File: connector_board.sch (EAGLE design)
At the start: 4 parts, among them X1 0446200002

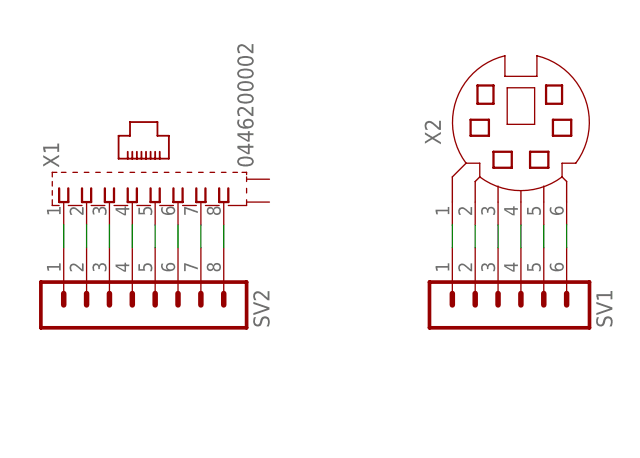
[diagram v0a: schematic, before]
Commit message: added PCBs for extern IO-connections
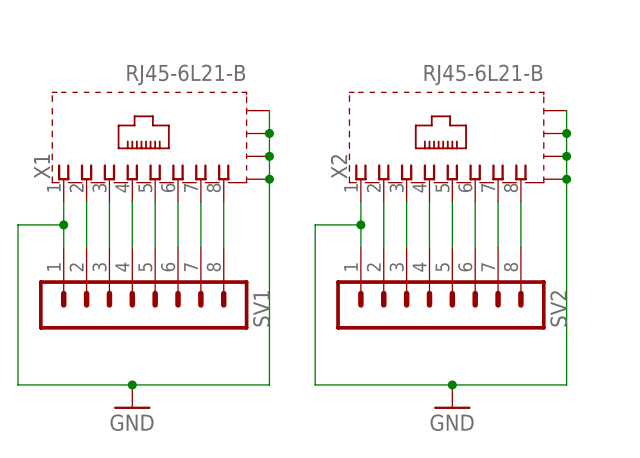
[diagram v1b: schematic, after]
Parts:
- SV1: device con-lstb:MA06-1 -> con-lstb:MA08-1
- X1: value 0446200002 -> RJ45-6L21-B; device con-molex:0446200002 -> con-tycoelectronics:RJ45-6L21-B
- X2: value (none) -> RJ45-6L21-B; device con-yamaichi:MD06SS -> con-tycoelectronics:RJ45-6L21-B
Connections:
- removed net N$1: SV1.1, X2.1
- removed net N$10: SV2.4, X1.4
- removed net N$2: SV1.2, X2.2
- removed net N$9: SV2.3, X1.3
- new net GND: SV1.1, SV2.1, X1.1, X1.S@1, X1.S@2, X1.S@3, X1.S@4, X2.1, X2.S@1, X2.S@2, X2.S@3, X2.S@4
- new net N$15: SV2.7, X2.7
- new net N$16: SV2.8, X2.8
- new net N$19: SV1.2, X1.2
- new net N$20: SV2.2, X2.2
- net N$11: now also SV2.3, X2.3; no longer SV2.5, X1.5
- net N$12: now also SV2.4, X2.4; no longer SV2.6, X1.6
- net N$13: now also SV2.5, X2.5; no longer SV2.7, X1.7
- net N$14: now also SV2.6, X2.6; no longer SV2.8, X1.8
- net N$3: now also X1.3; no longer X2.3
- net N$4: now also X1.4; no longer X2.4
- net N$5: now also X1.5; no longer X2.5
- net N$6: now also X1.6; no longer X2.6
- net N$7: now also SV1.7, X1.7; no longer SV2.1, X1.1
- net N$8: now also SV1.8, X1.8; no longer SV2.2, X1.2
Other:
- moved on the sheet: SV2
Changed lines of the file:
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@@
 </classes>
 <parts>
-<part name="X1" library="con-molex" deviceset="0446200002" device=""/>
-<part name="X2" library="con-yamaichi" deviceset="MD06SS" device=""/>
-<part name="SV1" library="con-lstb" deviceset="MA06-1" device=""/>
 <part name="SV2" library="con-lstb" deviceset="MA08-1" device=""/>
+<part name="SV1" library="con-lstb" deviceset="MA08-1" device=""/>
+<part name="X1" library="con-tycoelectronics" deviceset="RJ45*2" device="1-B" technology="-6L"/>
+<part name="X2" library="con-tycoelectronics" deviceset="RJ45*2" device="1-B" technology="-6L"/>
+<part name="GND1" library="supply1" deviceset="GND" device=""/>
+<part name="GND2" library="supply1" deviceset="GND" device=""/>
 </parts>
 <sheets>
@@
 </plain>
 <instances>
-<instance part="X1" gate="P" x="27.94" y="55.88" rot="R90"/>
-<instance part="X2" gate="G$1" x="68.58" y="63.5" rot="R90"/>
-<instance part="SV1" gate="1" x="68.58" y="43.18" rot="MR90"/>
-<instance part="SV2" gate="1" x="25.4" y="43.18" rot="MR90"/>
+<instance part="SV2" gate="1" x="58.42" y="43.18" rot="MR90"/>
+<instance part="SV1" gate="1" x="25.4" y="43.18" rot="MR90"/>
+<instance part="X1" gate="G$1" x="27.94" y="63.5" rot="R90"/>
+<instance part="X2" gate="G$1" x="60.96" y="63.5" rot="R90"/>
+<instance part="GND1" gate="1" x="25.4" y="33.02"/>
+<instance part="GND2" gate="1" x="60.96" y="33.02"/>
 </instances>
 <busses>
 </busses>
 <nets>
-<net name="N$1" class="0">
-<segment>
-<pinref part="X2" gate="G$1" pin="1"/>
-<pinref part="SV1" gate="1" pin="1"/>
-<wire x1="60.96" y1="50.8" x2="60.96" y2="53.34" width="0.1524" layer="91"/>
-</segment>
-</net>
-<net name="N$2" class="0">
-<segment>
-<pinref part="X2" gate="G$1" pin="2"/>
-<pinref part="SV1" gate="1" pin="2"/>
-<wire x1="63.5" y1="50.8" x2="63.5" y2="53.34" width="0.1524" layer="91"/>
-</segment>
-</net>
 <net name="N$3" class="0">
 <segment>
-<pinref part="X2" gate="G$1" pin="3"/>
 <pinref part="SV1" gate="1" pin="3"/>
-<wire x1="66.04" y1="50.8" x2="66.04" y2="53.34" width="0.1524" layer="91"/>
+<wire x1="22.86" y1="50.8" x2="22.86" y2="55.88" width="0.1524" layer="91"/>
+<pinref part="X1" gate="G$1" pin="3"/>
 </segment>
 </net>
 <net name="N$4" class="0">
 <segment>
-<pinref part="X2" gate="G$1" pin="4"/>
 <pinref part="SV1" gate="1" pin="4"/>
-<wire x1="68.58" y1="50.8" x2="68.58" y2="53.34" width="0.1524" layer="91"/>
+<wire x1="25.4" y1="50.8" x2="25.4" y2="55.88" width="0.1524" layer="91"/>
+<pinref part="X1" gate="G$1" pin="4"/>
 </segment>
 </net>
 <net name="N$5" class="0">
 <segment>
-<pinref part="X2" gate="G$1" pin="5"/>
 <pinref part="SV1" gate="1" pin="5"/>
-<wire x1="71.12" y1="50.8" x2="71.12" y2="53.34" width="0.1524" layer="91"/>
+<wire x1="27.94" y1="50.8" x2="27.94" y2="55.88" width="0.1524" layer="91"/>
+<pinref part="X1" gate="G$1" pin="5"/>
 </segment>
 </net>
 <net name="N$6" class="0">
 <segment>
-<pinref part="X2" gate="G$1" pin="6"/>
 <pinref part="SV1" gate="1" pin="6"/>
-<wire x1="73.66" y1="50.8" x2="73.66" y2="53.34" width="0.1524" layer="91"/>
+<wire x1="30.48" y1="50.8" x2="30.48" y2="55.88" width="0.1524" layer="91"/>
+<pinref part="X1" gate="G$1" pin="6"/>
 </segment>
 </net>
 <net name="N$7" class="0">
 <segment>
-<pinref part="X1" gate="P" pin="1"/>
-<pinref part="SV2" gate="1" pin="1"/>
-<wire x1="17.78" y1="50.8" x2="17.78" y2="53.34" width="0.1524" layer="91"/>
+<pinref part="SV1" gate="1" pin="7"/>
+<wire x1="33.02" y1="50.8" x2="33.02" y2="55.88" width="0.1524" layer="91"/>
+<pinref part="X1" gate="G$1" pin="7"/>
 </segment>
 </net>
 <net name="N$8" class="0">
 <segment>
-<pinref part="X1" gate="P" pin="2"/>
-<pinref part="SV2" gate="1" pin="2"/>
-<wire x1="20.32" y1="50.8" x2="20.32" y2="53.34" width="0.1524" layer="91"/>
-</segment>
-</net>
-<net name="N$9" class="0">
-<segment>
-<pinref part="X1" gate="P" pin="3"/>
-<pinref part="SV2" gate="1" pin="3"/>
-<wire x1="22.86" y1="50.8" x2="22.86" y2="53.34" width="0.1524" layer="91"/>
-</segment>
-</net>
-<net name="N$10" class="0">
-<segment>
-<pinref part="X1" gate="P" pin="4"/>
-<pinref part="SV2" gate="1" pin="4"/>
-<wire x1="25.4" y1="50.8" x2="25.4" y2="53.34" width="0.1524" layer="91"/>
+<pinref part="SV1" gate="1" pin="8"/>
+<wire x1="35.56" y1="50.8" x2="35.56" y2="55.88" width="0.1524" layer="91"/>
+<pinref part="X1" gate="G$1" pin="8"/>
 </segment>
 </net>
 <net name="N$11" class="0">
 <segment>
-<pinref part="X1" gate="P" pin="5"/>
-<pinref part="SV2" gate="1" pin="5"/>
-<wire x1="27.94" y1="50.8" x2="27.94" y2="53.34" width="0.1524" layer="91"/>
+<pinref part="SV2" gate="1" pin="3"/>
+<wire x1="55.88" y1="50.8" x2="55.88" y2="55.88" width="0.1524" layer="91"/>
+<pinref part="X2" gate="G$1" pin="3"/>
 </segment>
 </net>
 <net name="N$12" class="0">
 <segment>
-<pinref part="X1" gate="P" pin="6"/>
-<pinref part="SV2" gate="1" pin="6"/>
-<wire x1="30.48" y1="50.8" x2="30.48" y2="53.34" width="0.1524" layer="91"/>
+<pinref part="SV2" gate="1" pin="4"/>
+<wire x1="58.42" y1="50.8" x2="58.42" y2="55.88" width="0.1524" layer="91"/>
+<pinref part="X2" gate="G$1" pin="4"/>
 </segment>
 </net>
 <net name="N$13" class="0">
 <segment>
-<pinref part="X1" gate="P" pin="7"/>
-<pinref part="SV2" gate="1" pin="7"/>
-<wire x1="33.02" y1="50.8" x2="33.02" y2="53.34" width="0.1524" layer="91"/>
+<pinref part="SV2" gate="1" pin="5"/>
+<wire x1="60.96" y1="50.8" x2="60.96" y2="55.88" width="0.1524" layer="91"/>
+<pinref part="X2" gate="G$1" pin="5"/>
 </segment>
 </net>
 <net name="N$14" class="0">
 <segment>
-<pinref part="X1" gate="P" pin="8"/>
-<pinref part="SV2" gate="1" pin="8"/>
-<wire x1="35.56" y1="50.8" x2="35.56" y2="53.34" width="0.1524" layer="91"/>
+<pinref part="SV2" gate="1" pin="6"/>
+<wire x1="63.5" y1="50.8" x2="63.5" y2="55.88" width="0.1524" layer="91"/>
+<pinref part="X2" gate="G$1" pin="6"/>
 </segment>
 </net>
+<net name="N$15" class="0">
+<segment>
+<pinref part="SV2" gate="1" pin="7"/>
+<wire x1="66.04" y1="50.8" x2="66.04" y2="55.88" width="0.1524" layer="91"/>
+<pinref part="X2" gate="G$1" pin="7"/>
+</segment>
+</net>
+<net name="N$16" class="0">
+<segment>
+<pinref part="SV2" gate="1" pin="8"/>
+<wire x1="68.58" y1="50.8" x2="68.58" y2="55.88" width="0.1524" layer="91"/>
+<pinref part="X2" gate="G$1" pin="8"/>
+</segment>
+</net>
+<net name="N$19" class="0">
+<segment>
+<pinref part="SV1" gate="1" pin="2"/>
+<wire x1="20.32" y1="50.8" x2="20.32" y2="55.88" width="0.1524" layer="91"/>
+<pinref part="X1" gate="G$1" pin="2"/>
+</segment>
+</net>
+<net name="N$20" class="0">
+<segment>
+<pinref part="SV2" gate="1" pin="2"/>
+<wire x1="53.34" y1="50.8" x2="53.34" y2="55.88" width="0.1524" layer="91"/>
+<pinref part="X2" gate="G$1" pin="2"/>
+</segment>
+</net>
+<net name="GND" class="0">
+<segment>
+<wire x1="40.64" y1="58.42" x2="40.64" y2="60.96" width="0.1524" layer="91"/>
+<wire x1="40.64" y1="58.42" x2="40.64" y2="35.56" width="0.1524" layer="91"/>
+<junction x="40.64" y="58.42"/>
+<wire x1="40.64" y1="35.56" x2="25.4" y2="35.56" width="0.1524" layer="91"/>
+<wire x1="25.4" y1="35.56" x2="12.7" y2="35.56" width="0.1524" layer="91"/>
+<wire x1="12.7" y1="35.56" x2="12.7" y2="53.34" width="0.1524" layer="91"/>
+<pinref part="SV1" gate="1" pin="1"/>
+<wire x1="17.78" y1="50.8" x2="17.78" y2="53.34" width="0.1524" layer="91"/>
+<wire x1="17.78" y1="53.34" x2="17.78" y2="55.88" width="0.1524" layer="91"/>
+<wire x1="12.7" y1="53.34" x2="17.78" y2="53.34" width="0.1524" layer="91"/>
+<junction x="17.78" y="53.34"/>
+<pinref part="X1" gate="G$1" pin="S@2"/>
+<pinref part="X1" gate="G$1" pin="S@1"/>
+<pinref part="X1" gate="G$1" pin="1"/>
+<pinref part="X1" gate="G$1" pin="S@3"/>
+<wire x1="40.64" y1="60.96" x2="40.64" y2="63.5" width="0.1524" layer="91"/>
+<junction x="40.64" y="60.96"/>
+<pinref part="X1" gate="G$1" pin="S@4"/>
+<wire x1="40.64" y1="63.5" x2="40.64" y2="66.04" width="0.1524" layer="91"/>
+<junction x="40.64" y="63.5"/>
+<pinref part="GND1" gate="1" pin="GND"/>
+<junction x="25.4" y="35.56"/>
+</segment>
+<segment>
+<wire x1="73.66" y1="35.56" x2="73.66" y2="58.42" width="0.1524" layer="91"/>
+<wire x1="73.66" y1="58.42" x2="73.66" y2="60.96" width="0.1524" layer="91"/>
+<wire x1="73.66" y1="35.56" x2="60.96" y2="35.56" width="0.1524" layer="91"/>
+<wire x1="60.96" y1="35.56" x2="45.72" y2="35.56" width="0.1524" layer="91"/>
+<wire x1="45.72" y1="35.56" x2="45.72" y2="53.34" width="0.1524" layer="91"/>
+<pinref part="SV2" gate="1" pin="1"/>
+<wire x1="50.8" y1="50.8" x2="50.8" y2="53.34" width="0.1524" layer="91"/>
+<wire x1="50.8" y1="53.34" x2="50.8" y2="55.88" width="0.1524" layer="91"/>
+<wire x1="45.72" y1="53.34" x2="50.8" y2="53.34" width="0.1524" layer="91"/>
+<junction x="50.8" y="53.34"/>
+<pinref part="X2" gate="G$1" pin="S@2"/>
+<pinref part="X2" gate="G$1" pin="S@1"/>
+<junction x="73.66" y="58.42"/>
+<pinref part="X2" gate="G$1" pin="1"/>
+<pinref part="X2" gate="G$1" pin="S@3"/>
+<wire x1="73.66" y1="60.96" x2="73.66" y2="63.5" width="0.1524" layer="91"/>
+<junction x="73.66" y="60.96"/>
+<pinref part="X2" gate="G$1" pin="S@4"/>
+<wire x1="73.66" y1="63.5" x2="73.66" y2="66.04" width="0.1524" layer="91"/>
+<junction x="73.66" y="63.5"/>
+<pinref part="GND2" gate="1" pin="GND"/>
+<junction x="60.96" y="35.56"/>
+</segment>
+</net>
